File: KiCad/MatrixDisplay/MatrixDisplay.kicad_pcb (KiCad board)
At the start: 2 copper layers, 3 parts, among them J1 PUT_IN, J2 Power, U1 mini_esp32

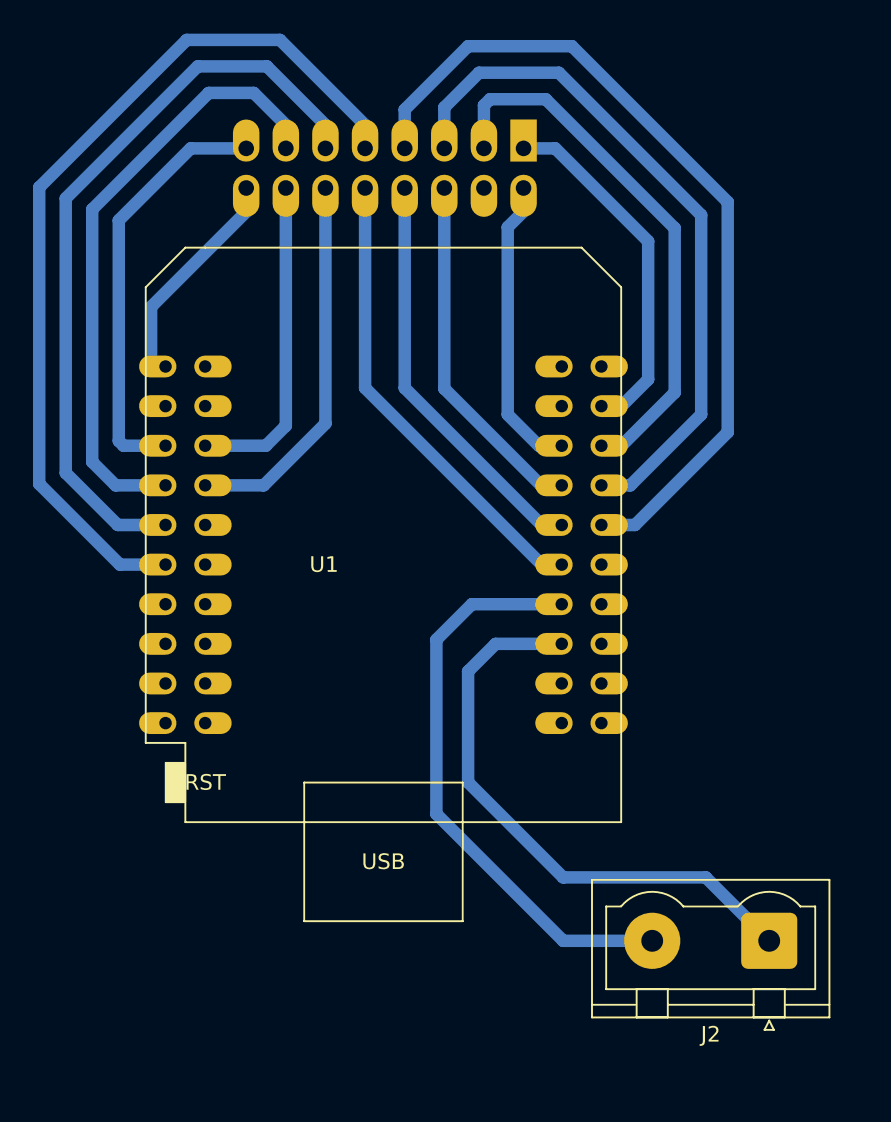
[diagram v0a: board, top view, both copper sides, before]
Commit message: updated pinout used for PCB Adapter
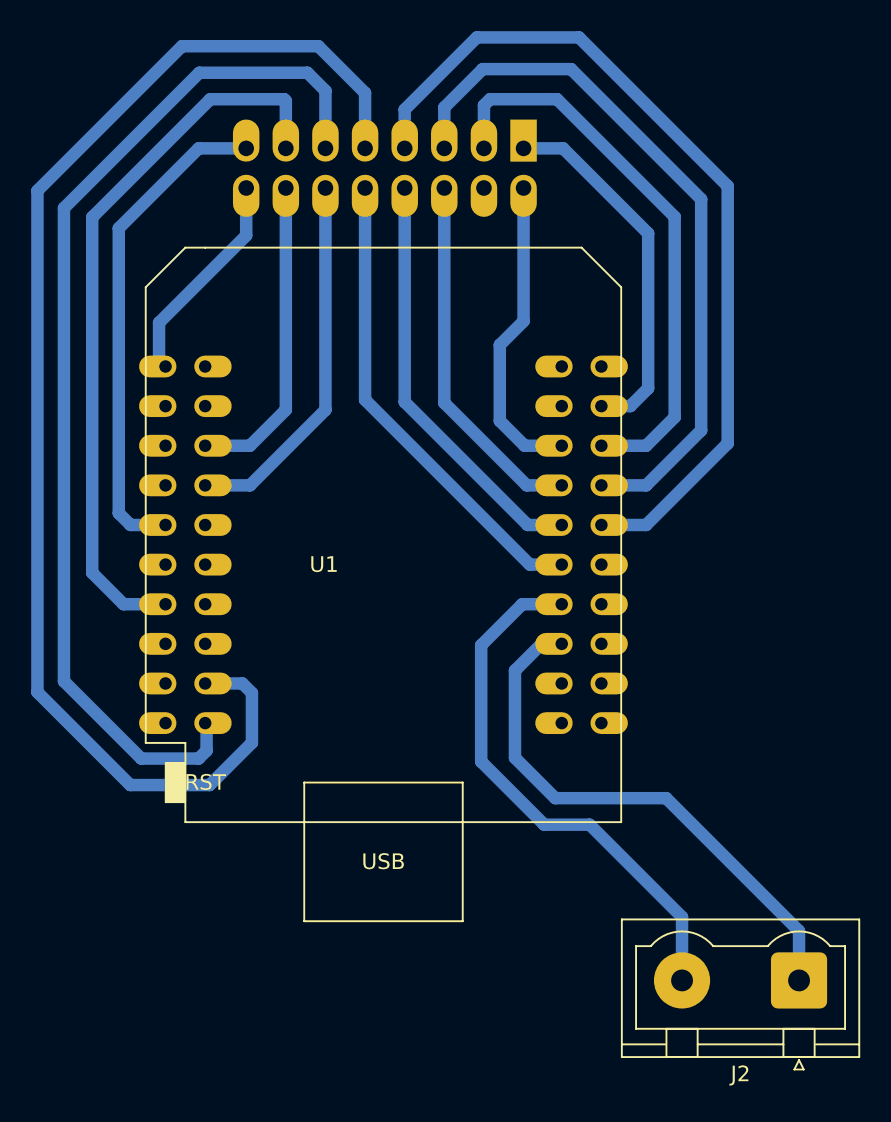
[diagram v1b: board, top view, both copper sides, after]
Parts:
- moved J2 3.18 mm to (151.3, 138.7)
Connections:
- J1 pad 11: Net-(U1-Pad9) -> Net-(U1-Pad20)
- J1 pad 13: Net-(U1-Pad7) -> Net-(U1-Pad13)
- J1 pad 15: Net-(J1-Pad15) -> Net-(U1-Pad9)
- J1 pad 9: Net-(U1-Pad11) -> Net-(U1-Pad18)
- U1 pad 11: Net-(U1-Pad11) -> unconnected-(U1-Pad11)
- U1 pad 13: unconnected-(U1-Pad13) -> Net-(U1-Pad13)
- U1 pad 18: unconnected-(U1-Pad18) -> Net-(U1-Pad18)
- U1 pad 20: unconnected-(U1-Pad20) -> Net-(U1-Pad20)
- U1 pad 5: Net-(J1-Pad15) -> unconnected-(U1-Pad5)
- U1 pad 7: Net-(U1-Pad7) -> unconnected-(U1-Pad7)
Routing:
- net Net-(U1-Pad18): track 0.00 -> 85.6 mm
- net Net-(U1-Pad20): track 0.00 -> 68.6 mm
- net Net-(U1-Pad11): track 57.8 -> 0.00 mm
- net Net-(U1-Pad13): track 0.00 -> 47.0 mm
- net Net-(U1-Pad7): track 39.4 -> 0.00 mm
- net Net-(J1-Pad15): track 27.3 -> 0.00 mm
- net Net-(U1-Pad9): track 48.6 -> 31.9 mm
- net Net-(J2-Pad1): track 37.4 -> 35.3 mm
- net Net-(J1-Pad16): track 50.6 -> 48.7 mm
- net Net-(J1-Pad7): track 54.3 -> 55.8 mm
- net Net-(J1-Pad5): track 44.9 -> 46.2 mm
- net Net-(J1-Pad3): track 35.2 -> 36.6 mm
- net Net-(J1-Pad2): track 19.2 -> 20.2 mm
- net Net-(J1-Pad1): track 23.0 -> 23.6 mm
- net Net-(J1-Pad14): track 20.9 -> 20.3 mm
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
